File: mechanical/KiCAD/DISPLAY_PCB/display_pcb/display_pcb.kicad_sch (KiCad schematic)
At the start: 48 parts, among them J1 USB_C_Receptacle_USB2.0_16P, J2 Conn_01x18_Socket, J3 Conn_01x01_Pin, J4 Conn_01x01_Pin, J5 Conn_01x02_Pin, Q1 AO3401A, U1 ESP32-S3-WROOM-1, U3 USBLC6-2P6, U4 TP4056-42-ESOP8, U5 TLV75733PDBV

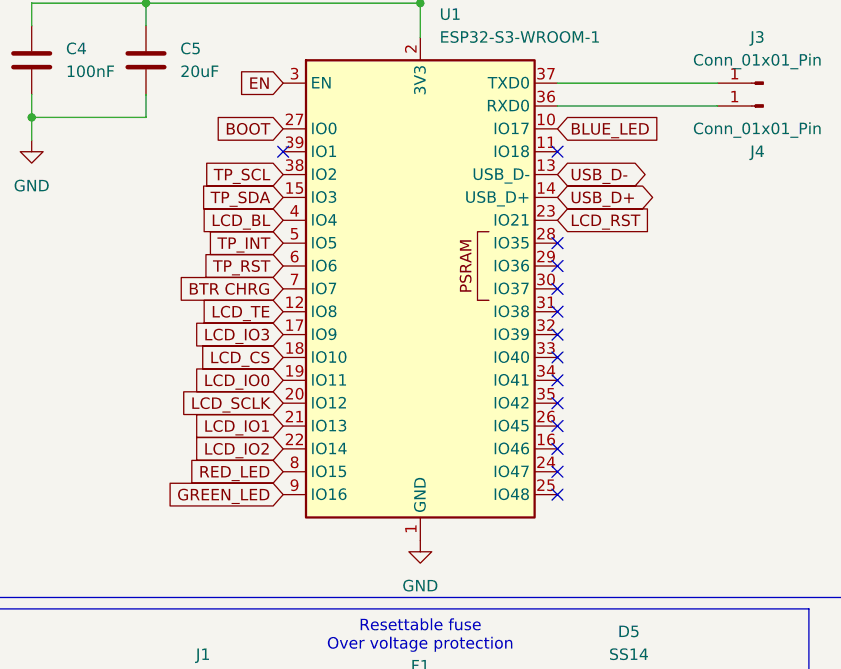
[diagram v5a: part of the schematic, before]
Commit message: Display PCB is basically finished, all routes are connected, all data lines should be within the length difference tolerance level, some spacing tolerances are still not fixed.
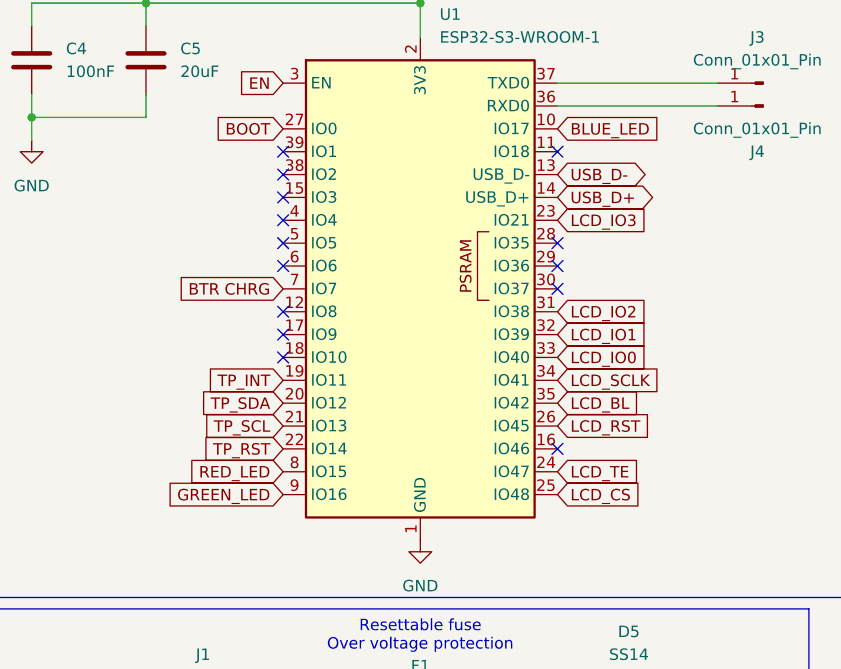
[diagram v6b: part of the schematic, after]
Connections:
- net LCD_BL: now also U1.35 (IO42); no longer U1.4 (IO4)
- net LCD_CS: now also U1.25 (IO48); no longer U1.18 (IO10)
- net LCD_IO0: now also U1.33 (IO40); no longer U1.19 (IO11)
- net LCD_IO1: now also U1.32 (IO39); no longer U1.21 (IO13)
- net LCD_IO2: now also U1.31 (IO38); no longer U1.22 (IO14)
- net LCD_IO3: now also U1.23 (IO21); no longer U1.17 (IO9)
- net LCD_RST: now also U1.26 (IO45); no longer U1.23 (IO21)
- net LCD_SCLK: now also U1.34 (IO41); no longer U1.20 (IO12)
- net LCD_TE: now also U1.24 (IO47); no longer U1.12 (IO8)
- net TP_INT: now also U1.19 (IO11); no longer U1.5 (IO5)
- net TP_RST: now also U1.22 (IO14); no longer U1.6 (IO6)
- net TP_SCL: now also U1.21 (IO13); no longer U1.38 (IO2)
- net TP_SDA: now also U1.20 (IO12); no longer U1.15 (IO3)

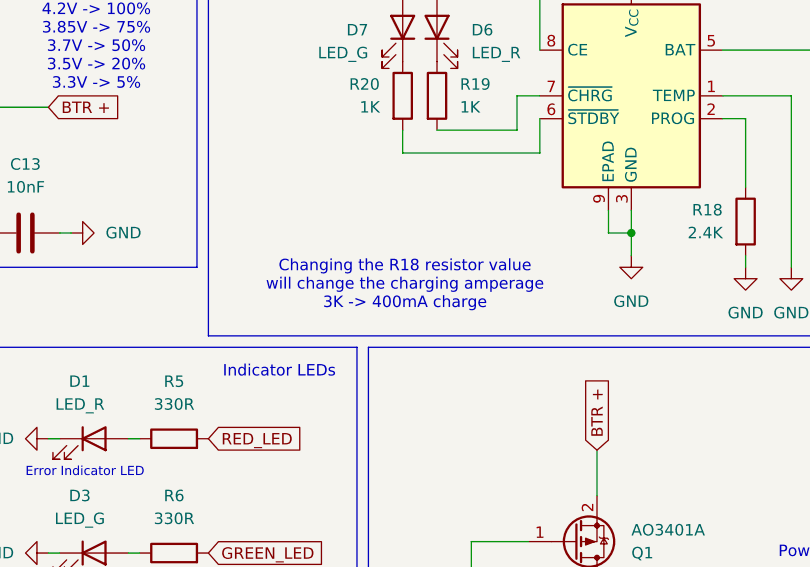
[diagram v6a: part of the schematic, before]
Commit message: OBD and displa PCB are both basically finished, some files has to be generated and the PCBs can be ordered. Documentation should be the next step.
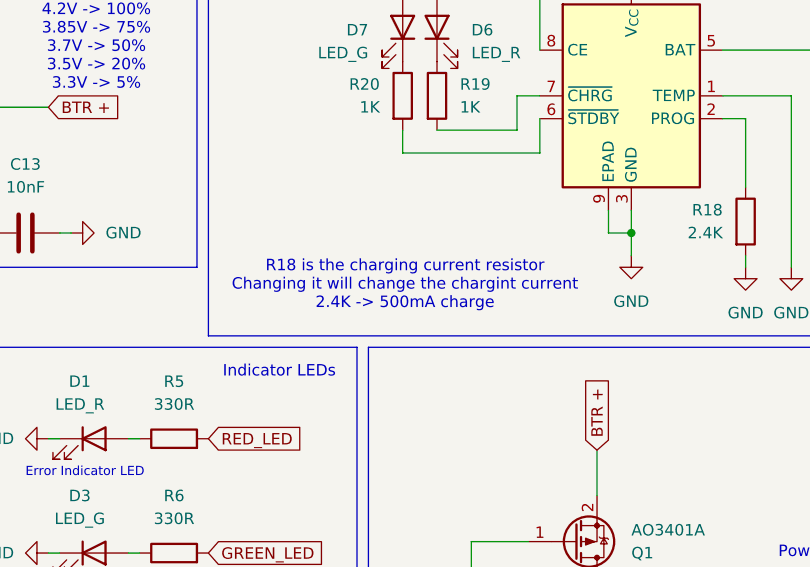
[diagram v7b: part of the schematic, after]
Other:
- note added: "R18 is the charging current resistor Changing it will change the chargint current 2.4K -> 500mA charge"
- note removed: "Changing the R18 resistor value will change the charging amperage 3K -> 400mA charge"
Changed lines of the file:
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@@
 		)
 	)
-	(text "Changing the R18 resistor value\nwill change the charging amperage\n3K -> 400mA charge"
+	(text "R18 is the charging current resistor\nChanging it will change the chargint current\n2.4K -> 500mA charge"
 		(exclude_from_sim no)
 		(at 216.154 97.282 0)

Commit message: PCBs should be finished, they can be ordered. The plan was to finish the PCB design about a week ago. I already have the display and got two ESP devboard so i can start the software and test it.
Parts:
- BOOT1, EN1: LCSC (none) -> C713480
- C10, C3, C7, C8, C9: LCSC (none) -> C14860
- C11, C4: LCSC (none) -> C1711
- C13: LCSC (none) -> C1710
- C2: LCSC (none) -> C50131
- C5: value 20uF -> 22uF; LCSC (none) -> C87996
- C6: footprint Capacitor_SMD:C_1206_3216Metric -> Capacitor_SMD:C_0805_2012Metric; LCSC (none) -> C1711
- D1, D6: LCSC (none) -> C84256
- D2: LCSC (none) -> C78401
- D3, D7: LCSC (none) -> C2297
- D4: LCSC (none) -> C2293
- D5, D8: LCSC (none) -> C2480
- F1: LCSC (none) -> C269104
- J1: LCSC (none) -> C165948
- J2: LCSC (none) -> C506792
- J3, J4: now left out of the parts list
- J5: LCSC (none) -> C177225
- Q1: LCSC (none) -> C15127
- R10, R8: LCSC (none) -> C17414
- R17, R23, R24: LCSC (none) -> C25611
- R18: LCSC (none) -> C17526
- R19, R20: LCSC (none) -> C17513
- R2, R3: LCSC (none) -> C27834
- R4: LCSC (none) -> C17927
- R5, R6, R7: footprint Resistor_SMD:R_0805_2012Metric -> Resistor_SMD:R_0603_1608Metric; LCSC (none) -> C23138
- R9: footprint Resistor_SMD:R_0805_2012Metric -> Resistor_SMD:R_0603_1608Metric; LCSC (none) -> C22775
- U1: LCSC (none) -> C2913201
- U3: LCSC (none) -> C2827693
- U4: LCSC (none) -> C16581
- U5: LCSC (none) -> C485517
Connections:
- net BTR -: no longer J5.2 (Pin_2)
- net GND: now also J5.2 (Pin_2)
